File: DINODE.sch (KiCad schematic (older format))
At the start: 18 parts

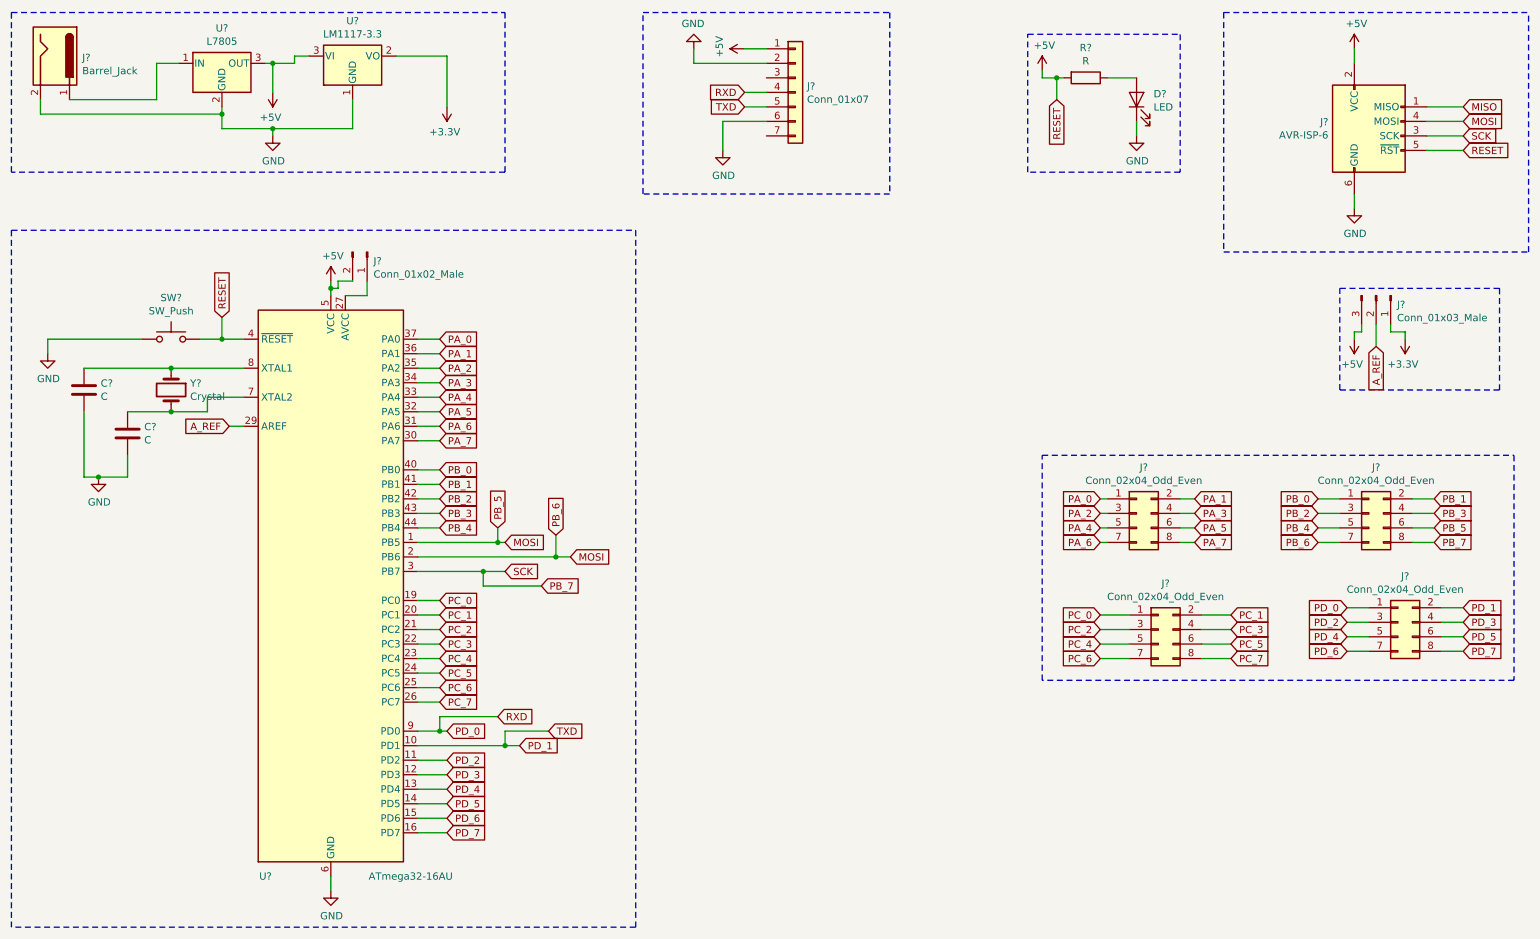
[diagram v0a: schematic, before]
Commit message: Addition of esp8266 connection to the circuit
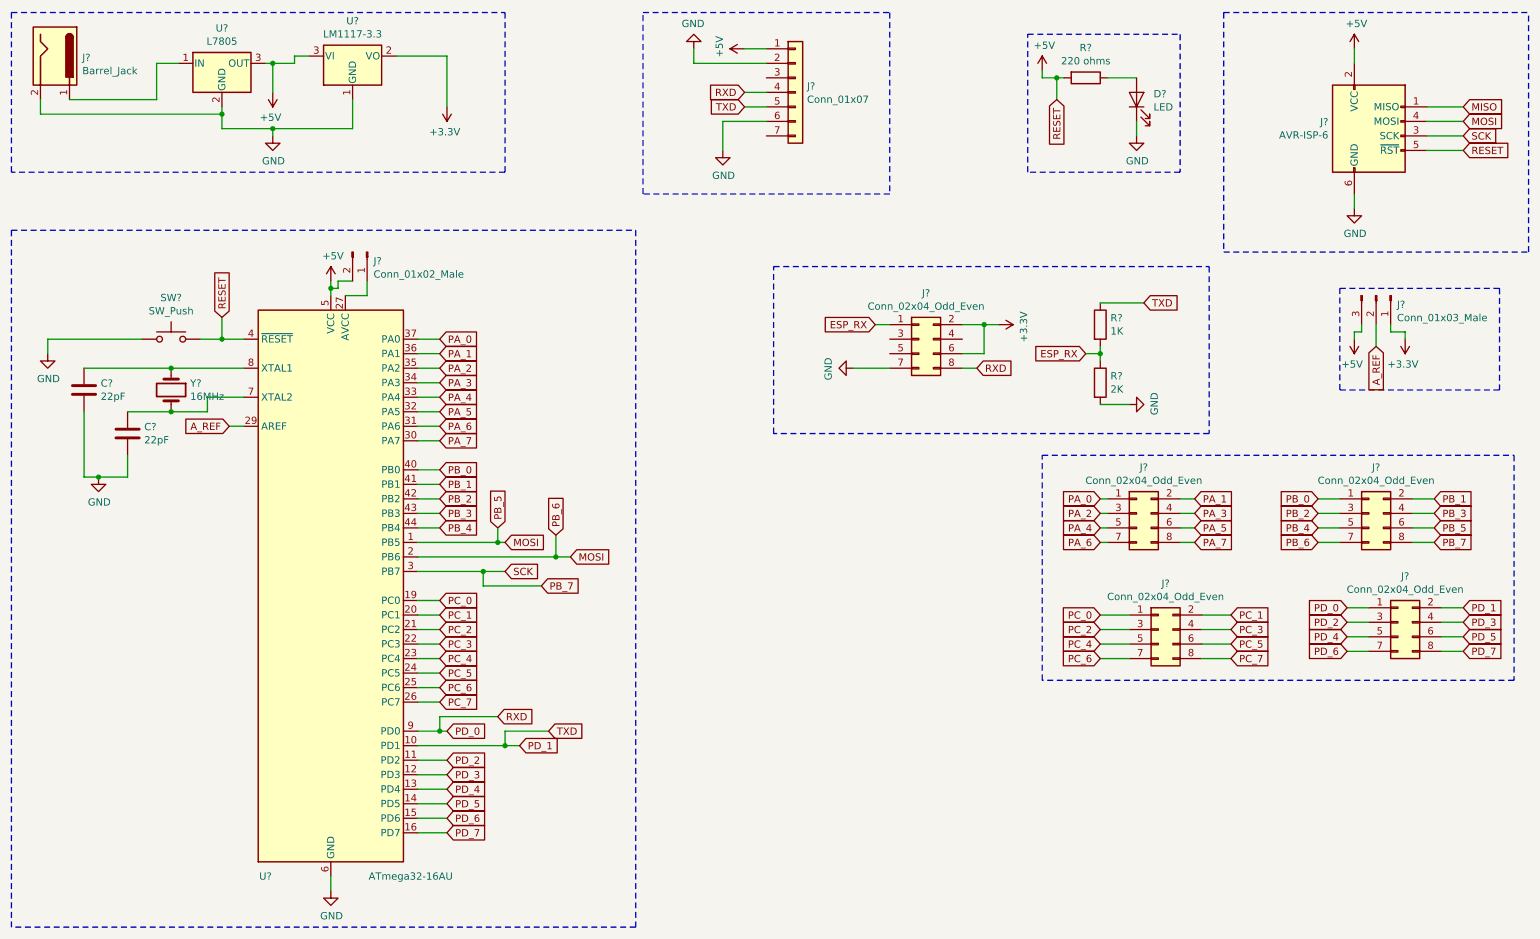
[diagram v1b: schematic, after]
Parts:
- added J?: Conn_02x04_Odd_Even, symbol Connector_Generic:Conn_02x04_Odd_Even
- added R?: 2K, symbol Device:R
- added R?: 1K, symbol Device:R
- C? (x2): value C -> 22pF
- R?: value R -> 220 ohms
- Y?: value Crystal -> 16MHz
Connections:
- net +3V3: now also J?.2 (Pin_2), J?.6 (Pin_6)
- net GND: now also J?.7 (Pin_7), R?.2
- net PD_0: now also J?.8 (Pin_8)
- net PD_1: now also R?.1
- new net ESP_RX: J?.1 (Pin_1), R?.1, R?.2
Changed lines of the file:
@@
 P 1050 3100
 F 0 "C?" H 1165 3146 50  0000 L CNN
-F 1 "C" H 1165 3055 50  0000 L CNN
+F 1 "22pF" H 1165 3055 50  0000 L CNN
 F 2 "" H 1088 2950 50  0001 C CNN
 F 3 "~" H 1050 3100 50  0001 C CNN
@@
 P 1350 3400
 F 0 "C?" H 1465 3446 50  0000 L CNN
-F 1 "C" H 1465 3355 50  0000 L CNN
+F 1 "22pF" H 1465 3355 50  0000 L CNN
 F 2 "" H 1388 3250 50  0001 C CNN
 F 3 "~" H 1350 3400 50  0001 C CNN
@@
 P 1650 3100
 F 0 "Y?" V 1604 3231 50  0000 L CNN
-F 1 "Crystal" V 1695 3231 50  0000 L CNN
+F 1 "16MHz" V 1695 3231 50  0000 L CNN
 F 2 "" H 1650 3100 50  0001 C CNN
 F 3 "~" H 1650 3100 50  0001 C CNN
@@
 P 7950 950
 F 0 "R?" V 7743 950 50  0000 C CNN
-F 1 "R" V 7834 950 50  0000 C CNN
+F 1 "220 ohms" V 7834 950 50  0000 C CNN
 F 2 "" V 7880 950 50  0001 C CNN
 F 3 "~" H 7950 950 50  0001 C CNN
@@
 RXD
 Wire Wire Line
-	3500 5450 3550 5450
-Wire Wire Line
-	3350 5450 3500 5450
-Connection ~ 3500 5450
-Wire Wire Line
-	3500 5350 3500 5450
-Wire Wire Line
-	3900 5350 3500 5350
-Wire Wire Line
 	3950 5550 4050 5550
 Wire Wire Line
@@
 Wire Notes Line
 	550  2000 550  6800
+$Comp
+L Connector_Generic:Conn_02x04_Odd_Even J?
+U 1 1 5DD2E808
+P 6800 2750
+F 0 "J?" H 6850 3067 50  0000 C CNN
+F 1 "Conn_02x04_Odd_Even" H 6850 2976 50  0000 C CNN
+F 2 "" H 6800 2750 50  0001 C CNN
+F 3 "~" H 6800 2750 50  0001 C CNN
+	1    6800 2750
+	1    0    0    -1
+$EndComp
+$Comp
+L power:+3.3V #PWR?
+U 1 1 5DD2FFA1
+P 7350 2650
+F 0 "#PWR?" H 7350 2500 50  0001 C CNN
+F 1 "+3.3V" H 7365 2823 50  0000 C CNN
+F 2 "" H 7350 2650 50  0001 C CNN
+F 3 "" H 7350 2650 50  0001 C CNN
+	1    7350 2650
+	0    1    1    0
+$EndComp
+Wire Wire Line
+	7100 2650 7250 2650
+Wire Wire Line
+	7100 2850 7250 2850
+Wire Wire Line
+	7250 2850 7250 2650
+Connection ~ 7250 2650
+Wire Wire Line
+	7250 2650 7350 2650
+$Comp
+L Device:R R?
+U 1 1 5DD41360
+P 8050 3050
+F 0 "R?" H 8120 3096 50  0000 L CNN
+F 1 "2K" H 8120 3005 50  0000 L CNN
+F 2 "" V 7980 3050 50  0001 C CNN
+F 3 "~" H 8050 3050 50  0001 C CNN
+	1    8050 3050
+	1    0    0    -1
+$EndComp
+$Comp
+L Device:R R?
+U 1 1 5DD4328D
+P 8050 2650
+F 0 "R?" H 8120 2696 50  0000 L CNN
+F 1 "1K" H 8120 2605 50  0000 L CNN
+F 2 "" V 7980 2650 50  0001 C CNN
+F 3 "~" H 8050 2650 50  0001 C CNN
+	1    8050 2650
+	1    0    0    -1
+$EndComp
+$Comp
+L power:GND #PWR?
+U 1 1 5DD4367C
+P 6350 2950
+F 0 "#PWR?" H 6350 2700 50  0001 C CNN
+F 1 "GND" H 6355 2777 50  0000 C CNN
+F 2 "" H 6350 2950 50  0001 C CNN
+F 3 "" H 6350 2950 50  0001 C CNN
+	1    6350 2950
+	0    1    1    0
+$EndComp
+Wire Wire Line
+	6350 2950 6600 2950
+$Comp
+L power:GND #PWR?
+U 1 1 5DD4B944
+P 8250 3200
+F 0 "#PWR?" H 8250 2950 50  0001 C CNN
+F 1 "GND" H 8255 3027 50  0000 C CNN
+F 2 "" H 8250 3200 50  0001 C CNN
+F 3 "" H 8250 3200 50  0001 C CNN
+	1    8250 3200
+	0    -1   -1   0
+$EndComp
+Wire Wire Line
+	8250 3200 8050 3200
+Wire Wire Line
+	8050 2900 8050 2850
+Text GLabel 8350 2500 2    50   Input ~ 0
+TXD
+Wire Wire Line
+	8050 2500 8350 2500
+Text GLabel 7950 2850 0    50   Input ~ 0
+ESP_RX
+Wire Wire Line
+	7950 2850 8050 2850
+Connection ~ 8050 2850
+Wire Wire Line
+	8050 2850 8050 2800
+Text GLabel 6500 2650 0    50   Input ~ 0
+ESP_RX
+Wire Wire Line
+	6500 2650 6600 2650
+Text GLabel 7200 2950 2    50   Input ~ 0
+RXD
+Wire Wire Line
+	7100 2950 7200 2950
+Wire Notes Line
+	5800 2250 8800 2250
+Wire Notes Line
+	8800 2250 8800 3400
+Wire Notes Line
+	8800 3400 5800 3400
+Wire Notes Line
+	5800 3400 5800 2250
+Wire Wire Line
+	3350 5450 3500 5450
+Wire Wire Line
+	3500 5450 3550 5450
+Connection ~ 3500 5450
+Wire Wire Line
+	3500 5350 3500 5450
+Wire Wire Line
+	3900 5350 3500 5350
 $EndSCHEMATC

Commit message: updated LCD layout
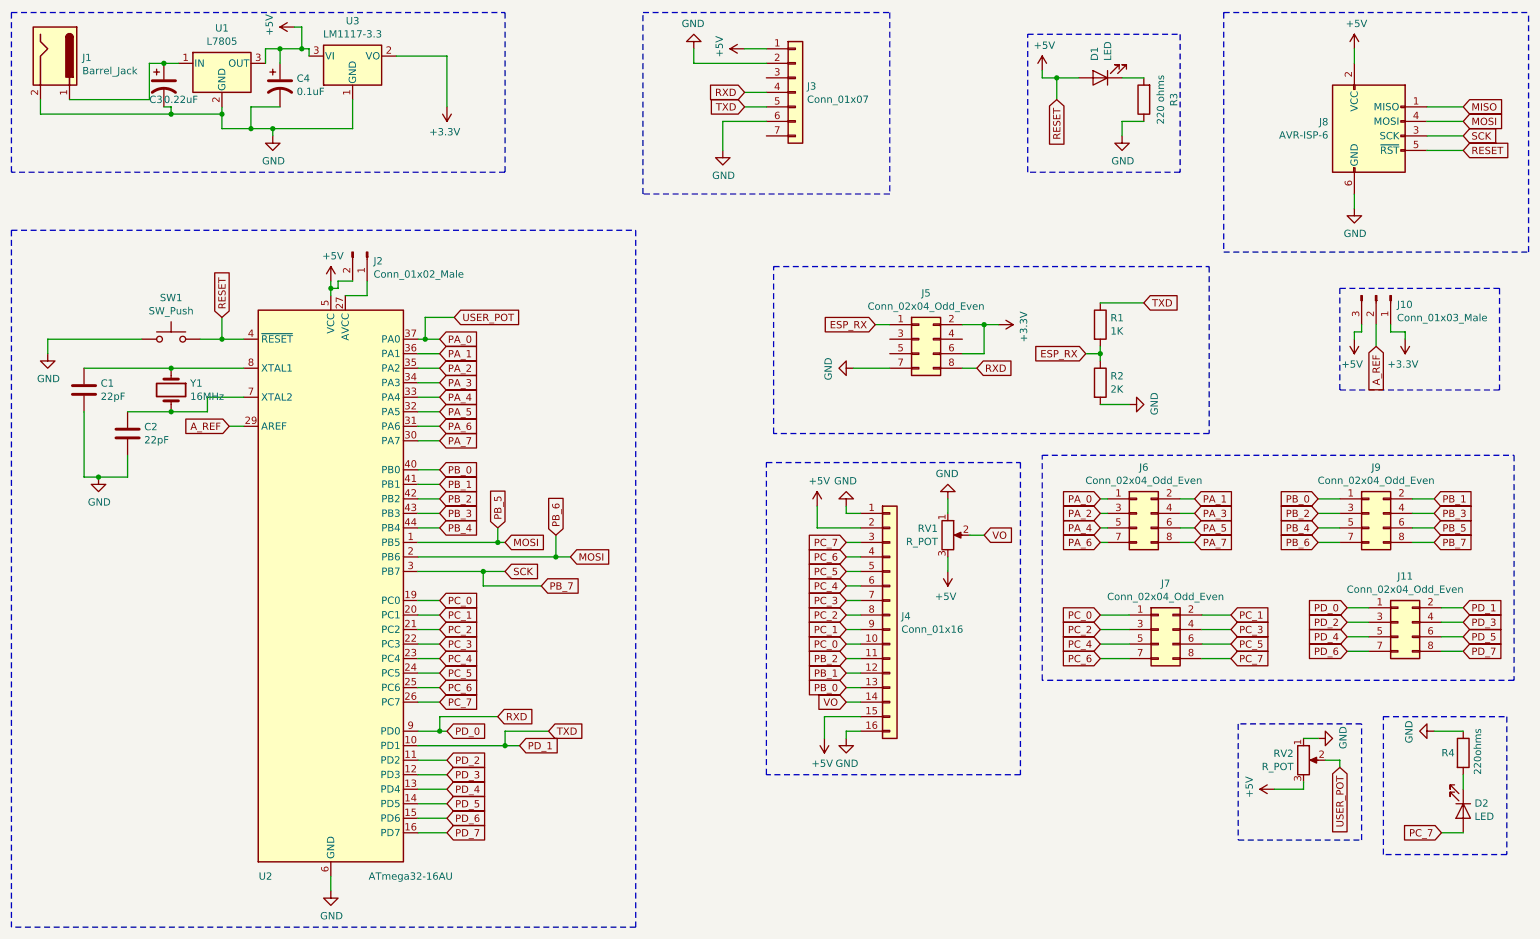
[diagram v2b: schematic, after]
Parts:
- added C3: 0.22uF, symbol Device:CP1
- added C4: 0.1uF, symbol Device:CP1
- added D2: LED, symbol Device:LED
- added J4: Conn_01x16, symbol Connector_Generic:Conn_01x16
- added R4: 220ohms, symbol Device:R
- added RV1, RV2: R_POT, symbol Device:R_POT
- gave numbers to parts that had none: 21
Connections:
- net +5V: now also D1.2 (A), C4.1, J4.15 (Pin_15), J4.2 (Pin_2), RV1.3, RV2.3; no longer R3.2
- net GND: now also R3.1, C3.2, C4.2, J4.1 (Pin_1), J4.16 (Pin_16), R4.1, RV1.1, RV2.1; no longer D1.1 (K)
- net PA_0: now also RV2.2
- net PB_0: now also J4.13 (Pin_13)
- net PB_1: now also J4.12 (Pin_12)
- net PB_2: now also J4.11 (Pin_11)
- net PC_0: now also J4.10 (Pin_10)
- net PC_1: now also J4.9 (Pin_9)
- net PC_2: now also J4.8 (Pin_8)
- net PC_3: now also J4.7 (Pin_7)
- net PC_4: now also J4.6 (Pin_6)
- net PC_5: now also J4.5 (Pin_5)
- net PC_6: now also J4.4 (Pin_4)
- net PC_7: now also D2.2 (A), J4.3 (Pin_3)
- net at J1.1, U1.1 (IN): now also C3.1
- new net: D1.1 (K), R3.2
- new net: D2.1 (K), R4.2
- new net VO: J4.14 (Pin_14), RV1.2
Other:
- moved on the sheet: D1, R3

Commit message: Updated circuit footprints
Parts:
- added C5, C6: 0.1uF, Capacitor_SMD:C_0805_2012Metric, symbol Device:C
- C1, C2: footprint (none) -> Capacitor_SMD:C_0805_2012Metric
- C3: value 0.22uF -> 100uF; footprint (none) -> Capacitor_THT:CP_Radial_D8.0mm_P5.00mm
- C4: value 0.1uF -> 10uF; footprint (none) -> Capacitor_THT:CP_Radial_D8.0mm_P5.00mm
- D1, D2: footprint (none) -> LED_THT:LED_D3.0mm
- J1: footprint (none) -> Connector_BarrelJack:BarrelJack_Horizontal
- J10: footprint (none) -> Connector_PinHeader_2.54mm:PinHeader_1x03_P2.54mm_Vertical
- J11, J6, J7, J9: footprint (none) -> Connector_PinHeader_2.54mm:PinHeader_2x04_P2.54mm_Horizontal
- J2: footprint (none) -> Connector_PinHeader_2.54mm:PinHeader_1x02_P2.54mm_Vertical
- J3: footprint (none) -> Connector_PinSocket_2.54mm:PinSocket_1x07_P2.54mm_Vertical
- J4: footprint (none) -> Connector_PinSocket_2.54mm:PinSocket_1x16_P2.54mm_Vertical
- J5: footprint (none) -> Connector_PinSocket_2.54mm:PinSocket_2x04_P2.54mm_Vertical
- J8: footprint (none) -> Connector_IDC:IDC-Header_2x03_P2.54mm_Horizontal
- R1, R2: footprint (none) -> Resistor_THT:R_Axial_DIN0207_L6.3mm_D2.5mm_P7.62mm_Horizontal
- R3, R4: footprint (none) -> Resistor_SMD:R_0805_2012Metric
- RV1, RV2: footprint (none) -> Potentiometer_THT:Potentiometer_Piher_PT-6-V_Vertical
- SW1: footprint (none) -> Button_Switch_THT:SW_PUSH_6mm_H4.3mm
- U1: footprint (none) -> digikey-footprints:TO-220-3
- U3: footprint (none) -> digikey-footprints:SOT-223
- Y1: footprint (none) -> Crystal:Crystal_HC49-U_Vertical
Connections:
- net +3V3: now also J5.4 (Pin_4), J5.8 (Pin_8); no longer J5.2 (Pin_2), J5.6 (Pin_6)
- net +5V: now also C6.1; no longer J8.5 (~RST), SW1.2, U2.4 (~RESET)
- net ESP_RX: now also J5.7 (Pin_7); no longer J5.1 (Pin_1)
- net GND: now also J5.1 (Pin_1), C5.2, C6.2; no longer J5.7 (Pin_7)
- net PD_0: now also J5.2 (Pin_2); no longer J5.8 (Pin_8)
- net at C3.1, J1.1, U1.1 (IN): now also C5.1
- new net: SW1.2, U2.4 (~RESET)
- new net RESET: J8.5 (~RST)
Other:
- moved on the sheet: C3, C4, U1
